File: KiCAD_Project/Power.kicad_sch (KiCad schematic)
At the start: 13 parts, among them J8 NP_Conn_01x02_Relief, J9 NP_Conn_01x02_Relief, U2 1-0000465, U3 1-0000576

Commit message: Issue #2 (NP on all XBEE parts, J3 changed to SMPL)
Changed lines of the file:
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@@
 (kicad_sch
-	(version 20231120)
+	(version 20250114)
 	(generator "eeschema")
-	(generator_version "8.0")
+	(generator_version "9.0")
 	(paper "USLetter")
 	(title_block
@@
 		(comment 2 "Gentry, AR 72734")
 		(comment 3 "23830 West AR Highway 12")
+	)
+	(text "Populate 0R0 and not debounce protection if desired."
+		(exclude_from_sim no)
+		(at 93.345 33.655 0)
+		(effects
+			(font
+				(size 1.27 1.27)
+			)
+			(justify left bottom)
+		)
+	)
+	(text "Delays turn on for approx 1 sec after\npower is applied to help with any\nswitch bounce/activation issues."
+		(exclude_from_sim no)
+		(at 153.035 43.18 0)
+		(effects
+			(font
+				(size 1.27 1.27)
+			)
+			(justify left bottom)
+		)
 	)
 	(junction
@@
 			"k+laF+QKAAACk4RocfgOqvQNL0QGAgBALBISrQq3Gf9cET3hHgAAgBRFq0KdQywM0CoAAEiHpEWr"
 			"wlMS2zYCpOUFAABAIA/RErCspStTZQSHUAEAQMpkKVoyQuk2TeD0AwCAvPh/UbNVz/ggVM8AAAAA"
-			"SUVORK5CYII="
-		)
-	)
-	(text "Populate 0R0 and not debounce protection if desired."
-		(exclude_from_sim no)
-		(at 93.345 33.655 0)
-		(effects
-			(font
-				(size 1.27 1.27)
-			)
-			(justify left bottom)
-		)
-	)
-	(text "Delays turn on for approx 1 sec after\npower is applied to help with any\nswitch bounce/activation issues."
-		(exclude_from_sim no)
-		(at 153.035 43.18 0)
-		(effects
-			(font
-				(size 1.27 1.27)
-			)
-			(justify left bottom)
-		)
-	)
+			"SUVORK5CYIKMADgDgAAAAAAAAAAACAAAAAAAAAAQG6K39gEAAAEAAAAAAAAAAAAAAAAAAABYfn+M"
+			"ADkDgAAAAAAAAAAACAAAAAAAAACQHaK39gEAAAEAAAAAAAAAAAAAAAAAAAAlfniMADoDgAAAAAAA"
+			"AAAAAwAAAAAAAAAgwKm39gEAAAEAAAAAAAAAAAAAAAAAAAAmfgWMADsDgFArqbf2AQAAAwAAAAAA"
+			"AAAgAKW39gEAAAEAAAAAAAAAAAAAAAAAAAAjfgaMADwDgMAhqbf2AQAAAwAAAAAAAADgAKW39gEA"
+			"AAEAAAAAAAAAAAAAAAAAAAAsfgOMAD0DgAAAAAAAAAAAAwAAAAAAAAAwKqm39gEAAAEAAAAAAAAA"
+			"AAAAAAAAAAApfgyMAD4DgAAtqbf2AQAAAwAAAAAAAADAvKm39gEAAAEAAAAAAAAAAAAAAAAAAAAq"
+			"fgmMAD8DgIAiqbf2AQAAAwAAAAAAAACg+qS39gEAAAEAAAAAAAAAAAAAAAAAAAA3fgqMAEADgAAA"
+			"AAAAAAAABAAAAAAAAAABAAAAAAAAAAEAAAAAAAAAAAAAAAAAAAAwfheMAEEDgAAAAAAAAAAAAwAA"
+			"AAAAAAAwvam39gEAAAEAAAAAAAAAAAAAAAAAAAA9fhCMAEIDgAAAAAAAAAAAAwAAAAAAAAAwMKm3"
+			"9gEAAAEAAAAAAAAAAAAAAAAAAAA+fh2MAEMDgCA0qbf2AQAAAwAAAAAAAAAA/KS39gEAAAEAAAAA"
+			"AAAAAAAAAAAAAAA7fh6MAEQDgAA5qbf2AQAAAwAAAAAAAAAA+6S39gEAAAEAAAAAAAAAAAAAAAAA"
+			"AAAEfhuMAEUDgIA0qbf2AQAAAwAAAAAAAADA/KS39gEAAAEAAAAAAAAAAAAAAAAAAAABfiSMAEYD"
+			"gAAAAAAAAAAACAAAAAAAAACQGKK39gEAAAEAAAAAAAAAAAAAAAAAAAACfiGMAEcDgAAAAAAAAAAA"
+			"AwAAAAAAAADgAaW39gEAAAEAAAAAAAAAAAAAAAAAAAAPfiKMAEgDgEM6L1dJTkRPV1MvZm9udHNc"
+			"TklBR0VORy5UVEYAAAAAAAAAAAAAAAAIfi+MAEkDgAAAAAAAAAAABAAAAAAAAAABAAAAAAAAAAEA"
+			"AAAAAAAAAAAAAAAAAAAVfiiMAEoDgAAAAAAAAAAAAwAAAAAAAAAwxKm39gEAAAEAAAAAAAAAAAAA"
+			"AAAAAAAWfjWMAEsDgJAzqbf2AQAAAwAAAAAAAABAvam39gEAAAEAAAAAAAAAAAAAAAAAAAATfjaM"
+			"AEwDgCAuqbf2AQAAAwAAAAAAAABA/KS39gEAAAEAAAAAAAAAAAAAAAAAAAAcfjOMAE0DgAAAAAAA"
+			"AAAABAAAAA=="
+		)
+	)

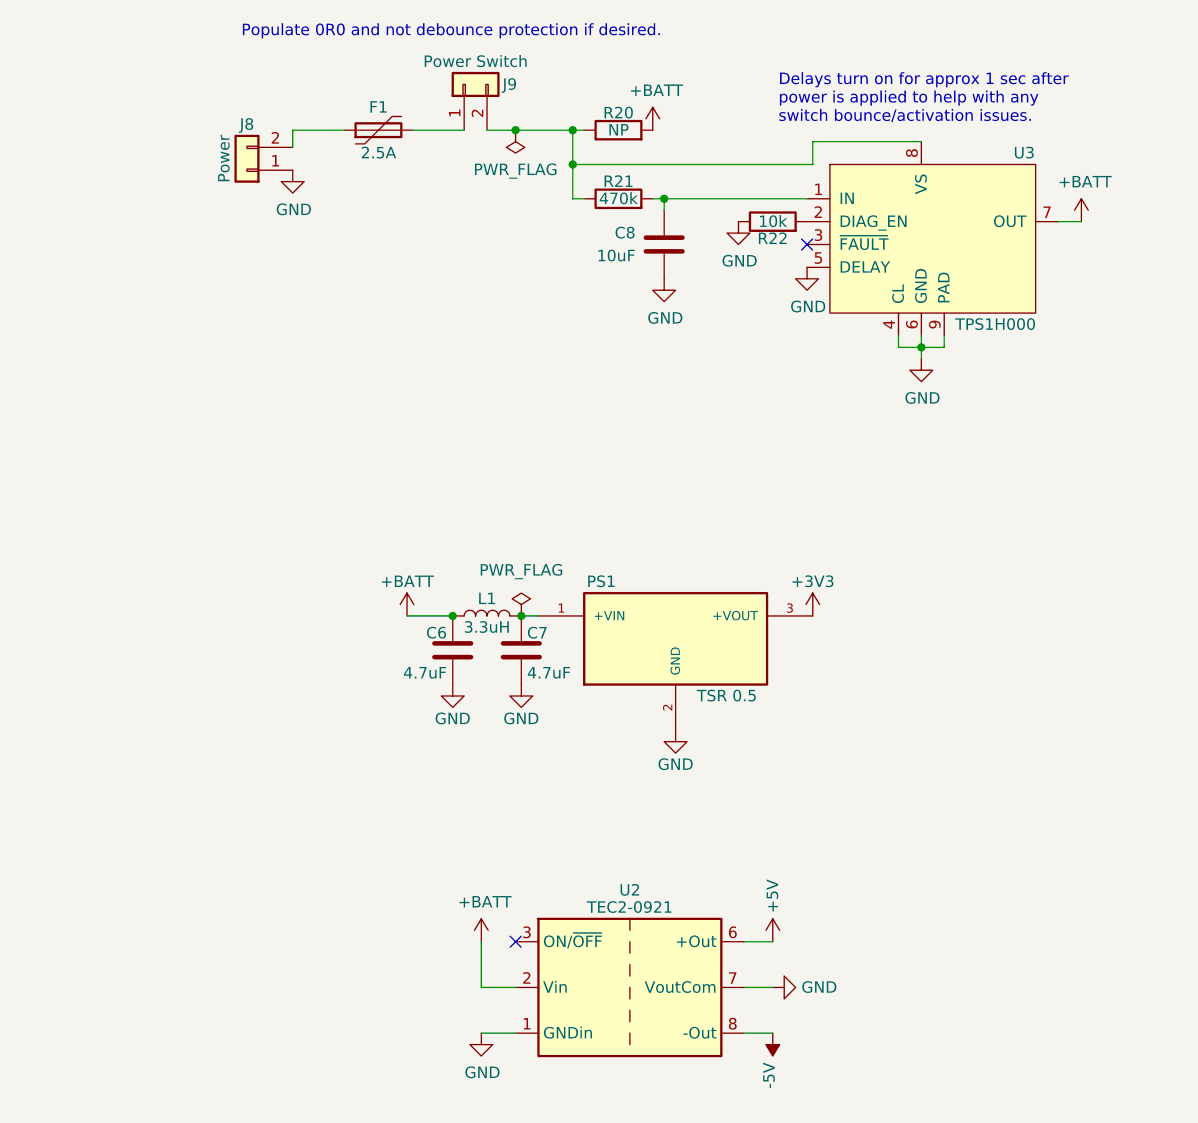
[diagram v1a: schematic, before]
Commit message: Fixed Issue #9 (Added RP Protection)
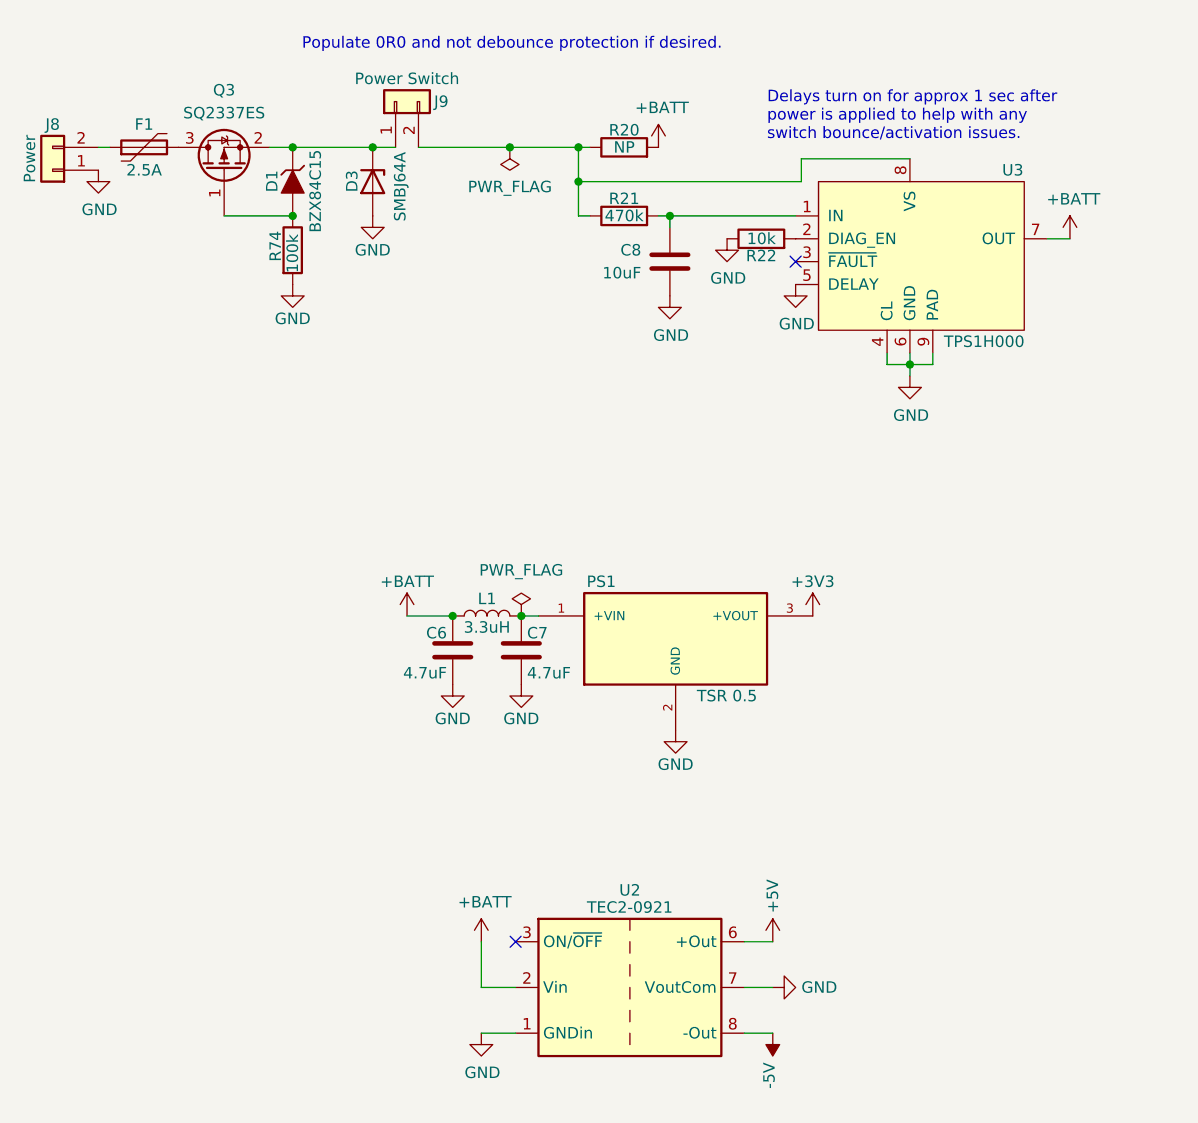
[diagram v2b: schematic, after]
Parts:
- added D1: 1-0001672, diodes:1-0001672, symbol diodes:1-0001672
- added D3: 1-0001537, diodes:1-0001537, symbol diodes:1-0001537
- added Q3: 1-0001670, mosfets:1-0001670, symbol mosfets:1-0001670
- added R74: 1-0000174, resistors_0603:1-0000174, symbol resistors_0603:1-0000174
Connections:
- net GND: now also D3.2 (A), R74.2
- net at F1.2: now also Q3.3 (D); no longer J9.1 (Pin_1)
- new net: D1.1 (A), Q3.1 (G), R74.1
- new net: D1.3 (K), D3.1 (K), J9.1 (Pin_1), Q3.2 (S)
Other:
- moved on the sheet: C8, F1, J8, J9, R20, R21, R22, U3

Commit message: Revised Layout for Rev2.0 Changes
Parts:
- renumbered D3 to D2, J9 to J10, J8 to J9, Q3 to Q1, R74 to R19
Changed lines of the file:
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@@
 	(title_block
 		(title "Digital Rotating Elextronics - NSSL EFM")
-		(date "2024-03-14")
-		(rev "1.0.0")
+		(date "2025-06-10")
+		(rev "2.0.0")
 		(company "Leeman Geophysical LLC")
 		(comment 1 "(479) 373-3736")
@@
 			"AAAAAAAAAAAAAAAAAAAAAAAAAAAAAAAAAKhu1zR+AgAA0NDuTX4CAAAgwhY8fgIAAAAAAAAAAAAA"
 			"AAAAAAAAAAAAAAAAAAAAAAcAAAAAAAAAAAAAAAAAAAAAAAAAAAAAAAAAAAAAAAAAAAAAAAAAAAAA"
-			"AAAAAAAAAA=="
+			"AAAAAAAAAABLlpD3AQAAAAAAAAAAAAAAAAAAAAAAAA8AAAAAAAAAAFCWkPcBAAAAAAAAAAAAAAAA"
+			"AAAAAAAADwAAAAAAAAAAcmlhbCBOYXJyb3cAAAAAAAAAAAAAAAAPAAAAAAAAAAAAAAAAAAAAAAAA"
+			"AAAAAAAAAAAAAAAAAABflpD3AQAAAAAAAAAAAAAAAAAAAAAAAA8AAAAAAAAAAGFycm93IEl0YWxp"
+			"YwAAAAAAAAAAAAAADwAAAAAAAAAAcmlhbCBOYXJyb3cAAAAAAAAAAAAAAAAPAAAAAAAAAAAAAAAA"
+			"AAAAAAAAAAAAAAAAAAAAAAAAAABXlpD3AQAAAAAAAAAAAAAAAAAAAAAAAA8AAAAAAAAAAGFycm93"
+			"AAAAAAAAAAAAAAAAAAAAAAAADwAAAAAAAAAAcmlhbCBOYXJyb3cAAAAAAAAAAAAAAAAPAAAAAAAA"
+			"AAAAAAAAAAAAAAAAAAAAAAAAAAAAAAAAAABOVZD3AQAAAAAAAAAAAAAAAAAAAAAAAA8AAAAAAAAA"
+			"AGFycm93IEJvbGQAAAAAAAAAAAAAAAAADwAAAAAAAAAAcmlhbCBOYXJyb3cAAAAAAAAAAAAAAAAP"
+			"AAAAAAAAAAAAAAAAAAAAAAAAAAAAAAAAAAAAAAAAAADAVJD3AQAAAAAAAAAAAAAAAAAAAAAAAA8A"
+			"AAAAAAAAAMBUkPcBAAAAAAAAAAAAAAAAAAAAAAAADwAAAAAAAAAAcmlhbCBOYXJyb3cAAAAAAAAA"
+			"AAAAAAAPAAAAAAAAAAAAAAAAAAAAAAAAAAAAAAAAAAAAAAAAAAC7VJD3AQAAAAAAAAAAAAAAAAAA"
+			"AAAAAA8AAAAAAAAAAGFycm93IEl0YWxpYwAAAAAAAAAAAAAADwAAAAAAAAAAcmlhbCBOYXJyb3cA"
+			"AAAAAAAAAAAAAAAPAAAAAAAAAAAAAAAAAAAAAAAAAAAAAAAAAAAAAAAAAADLVJD3AQAAAAAAAAAA"
+			"AAAAAAAAAAAAAA8AAAAAAAAAAGFycm93AAAAAAAAAAAAAAAAAAAAAAAADwAAAAAAAAAAcmlhbCBO"
+			"YXJyb3cAAAAAAAAAAAAAAAAPAAAAAAAAAAAAAAAAAAAAAAAAAAAAAAAAAAAAAAAAAABWapD3AQAA"
+			"AAAAAAAAAAAAAAAAAAAAAA8AAAAAAAAAAGFycm93IEJvbGQAAAAAAAAAAAAAAAAADwAAAAAAAAAA"
+			"cmlhbCBOYXJyb3cAAAAAAAAAAAAAAAAPAAAAAAAAAAAAAAAAAAAAAAAAAAAAAAAAAAAAAAAAAACW"
+			"apD3AQAAAAAAAAAAAAAAAAAAAAAAAA8AAAAAAAAAAJdqkPcBAAAAAAAAAAAAAAAAAAAAAAAADwAA"
+			"AAAAAAAAcg=="
 		)
 	)
@@
 		(on_board yes)
 		(dnp no)
-		(property "Reference" "#PWR036"
+		(property "Reference" "#PWR038"
 			(at 111.76 101.6 0)
 			(effects
@@
 			(project "Digital_PCB"
 				(path "/3dbf31f8-25b6-4bae-a8a1-93cabd4e019f/7b8e0205-645d-4360-8e88-d4935c6dfdaa"
-					(reference "#PWR036")
+					(reference "#PWR038")
 					(unit 1)
 				)
@@
 		(on_board yes)
 		(dnp no)
-		(property "Reference" "#PWR047"
+		(property "Reference" "#PWR049"
 			(at 152.4 146.685 0)
 			(effects
@@
 			(project "Digital_PCB"
 				(path "/3dbf31f8-25b6-4bae-a8a1-93cabd4e019f/7b8e0205-645d-4360-8e88-d4935c6dfdaa"
-					(reference "#PWR047")
+					(reference "#PWR049")
 					(unit 1)
 				)
@@
 		(on_board yes)
 		(dnp no)
-		(property "Reference" "#PWR039"
+		(property "Reference" "#PWR041"
 			(at 120.015 150.495 0)
 			(effects
@@
 			(project "Digital_PCB"
 				(path "/3dbf31f8-25b6-4bae-a8a1-93cabd4e019f/7b8e0205-645d-4360-8e88-d4935c6dfdaa"
-					(reference "#PWR039")
+					(reference "#PWR041")
 					(unit 1)
 				)
@@
 		(on_board yes)
 		(dnp no)
-		(property "Reference" "#PWR049"
+		(property "Reference" "#PWR050"
 			(at 154.94 67.31 0)
 			(effects
@@
 			(project "Digital_PCB"
 				(path "/3dbf31f8-25b6-4bae-a8a1-93cabd4e019f/7b8e0205-645d-4360-8e88-d4935c6dfdaa"
-					(reference "#PWR049")
+					(reference "#PWR050")
 					(unit 1)
 				)
@@
 		(on_board yes)
 		(dnp no)
-		(property "Reference" "#PWR043"
+		(property "Reference" "#PWR044"
 			(at 140.97 68.58 0)
 			(effects
@@
 			(project "Digital_PCB"
 				(path "/3dbf31f8-25b6-4bae-a8a1-93cabd4e019f/7b8e0205-645d-4360-8e88-d4935c6dfdaa"
-					(reference "#PWR043")
+					(reference "#PWR044")
 					(unit 1)
 				)
@@
 		(on_board yes)
 		(dnp no)
-		(property "Reference" "R74"
+		(property "Reference" "R19"
 			(at 97.155 58.42 90)
 			(effects
@@
 			(project "Digital_PCB"
 				(path "/3dbf31f8-25b6-4bae-a8a1-93cabd4e019f/7b8e0205-645d-4360-8e88-d4935c6dfdaa"
-					(reference "R74")
+					(reference "R19")
 					(unit 1)
 				)
@@
 		(on_board yes)
 		(dnp no)
-		(property "Reference" "#PWR044"
+		(property "Reference" "#PWR046"
 			(at 147.32 62.23 0)
 			(effects
@@
 			(project "Digital_PCB"
 				(path "/3dbf31f8-25b6-4bae-a8a1-93cabd4e019f/7b8e0205-645d-4360-8e88-d4935c6dfdaa"
-					(reference "#PWR044")
+					(reference "#PWR046")
 					(unit 1)
 				)
@@
 		(on_board yes)
 		(dnp no)
-		(property "Reference" "#PWR041"
+		(property "Reference" "#PWR045"
 			(at 141.605 116.84 0)
 			(effects
@@
 			(project "Digital_PCB"
 				(path "/3dbf31f8-25b6-4bae-a8a1-93cabd4e019f/7b8e0205-645d-4360-8e88-d4935c6dfdaa"
-					(reference "#PWR041")
+					(reference "#PWR045")
 					(unit 1)
 				)
@@
 		(on_board yes)
 		(dnp no)
-		(property "Reference" "#PWR050"
+		(property "Reference" "#PWR052"
 			(at 167.64 77.47 0)
 			(effects
@@
 			(project "Digital_PCB"
 				(path "/3dbf31f8-25b6-4bae-a8a1-93cabd4e019f/7b8e0205-645d-4360-8e88-d4935c6dfdaa"
-					(reference "#PWR050")
+					(reference "#PWR052")
 					(unit 1)
 				)
@@
 		(on_board yes)
 		(dnp no)
-		(property "Reference" "#PWR037"
+		(property "Reference" "#PWR039"
 			(at 116.84 111.76 0)
 			(effects
@@
 			(project "Digital_PCB"
 				(path "/3dbf31f8-25b6-4bae-a8a1-93cabd4e019f/7b8e0205-645d-4360-8e88-d4935c6dfdaa"
-					(reference "#PWR037")
+					(reference "#PWR039")
 					(unit 1)
 				)
@@
 		(on_board yes)
 		(dnp no)
-		(property "Reference" "#PWR038"
+		(property "Reference" "#PWR040"
 			(at 120.015 137.795 0)
 			(effects
@@
 			(project "Digital_PCB"
 				(path "/3dbf31f8-25b6-4bae-a8a1-93cabd4e019f/7b8e0205-645d-4360-8e88-d4935c6dfdaa"
-					(reference "#PWR038")
+					(reference "#PWR040")
 					(unit 1)
 				)
@@
 		(on_board yes)
 		(dnp no)
-		(property "Reference" "#FLG01"
+		(property "Reference" "#FLG02"
 			(at 123.19 47.625 0)
 			(effects
@@
 			(project "Digital_PCB"
 				(path "/3dbf31f8-25b6-4bae-a8a1-93cabd4e019f/7b8e0205-645d-4360-8e88-d4935c6dfdaa"
-					(reference "#FLG01")
+					(reference "#FLG02")
 					(unit 1)
 				)
@@
 		(on_board yes)
 		(dnp no)
-		(property "Reference" "#PWR053"
+		(property "Reference" "#PWR036"
 			(at 99.06 67.31 0)
 			(effects
@@
 			(project "Digital_PCB"
 				(path "/3dbf31f8-25b6-4bae-a8a1-93cabd4e019f/7b8e0205-645d-4360-8e88-d4935c6dfdaa"
-					(reference "#PWR053")
+					(reference "#PWR036")
 					(unit 1)
 				)
@@
 		(on_board yes)
 		(dnp no)
-		(property "Reference" "D3"
+		(property "Reference" "D2"
 			(at 105.664 48.26 0)
 			(effects
@@
 			(project "Digital_PCB"
 				(path "/3dbf31f8-25b6-4bae-a8a1-93cabd4e019f/7b8e0205-645d-4360-8e88-d4935c6dfdaa"
-					(reference "D3")
+					(reference "D2")
 					(unit 1)
 				)
@@
 		(on_board yes)
 		(dnp no)
-		(property "Reference" "#PWR046"
+		(property "Reference" "#PWR048"
 			(at 158.75 139.065 0)
 			(effects
@@
 			(project "Digital_PCB"
 				(path "/3dbf31f8-25b6-4bae-a8a1-93cabd4e019f/7b8e0205-645d-4360-8e88-d4935c6dfdaa"
-					(reference "#PWR046")
+					(reference "#PWR048")
 					(unit 1)
 				)
@@
 		(on_board yes)
 		(dnp no)
-		(property "Reference" "Q3"
+		(property "Reference" "Q1"
 			(at 91.44 39.37 90)
 			(effects
@@
 			(project "Digital_PCB"
 				(path "/3dbf31f8-25b6-4bae-a8a1-93cabd4e019f/7b8e0205-645d-4360-8e88-d4935c6dfdaa"
-					(reference "Q3")
+					(reference "Q1")
 					(unit 1)
 				)
@@
 		(on_board yes)
 		(dnp no)
-		(property "Reference" "#PWR042"
+		(property "Reference" "#PWR043"
 			(at 139.7 49.53 0)
 			(effects
@@
 			(project "Digital_PCB"
 				(path "/3dbf31f8-25b6-4bae-a8a1-93cabd4e019f/7b8e0205-645d-4360-8e88-d4935c6dfdaa"
-					(reference "#PWR042")
+					(reference "#PWR043")
 					(unit 1)
 				)
@@
 		(on_board yes)
 		(dnp no)
-		(property "Reference" "J9"
+		(property "Reference" "J10"
 			(at 115.57 40.64 90)
 			(effects
@@
 			(project "Digital_PCB"
 				(path "/3dbf31f8-25b6-4bae-a8a1-93cabd4e019f/7b8e0205-645d-4360-8e88-d4935c6dfdaa"
-					(reference "J9")
+					(reference "J10")
 					(unit 1)
 				)
@@
 		(on_board yes)
 		(dnp no)
-		(property "Reference" "J8"
+		(property "Reference" "J9"
 			(at 72.39 43.18 0)
 			(effects
@@
 			(project "Digital_PCB"
 				(path "/3dbf31f8-25b6-4bae-a8a1-93cabd4e019f/7b8e0205-645d-4360-8e88-d4935c6dfdaa"
-					(reference "J8")
+					(reference "J9")
 					(unit 1)
 				)
@@
 		(on_board yes)
 		(dnp no)
-		(property "Reference" "#PWR048"
+		(property "Reference" "#PWR051"
 			(at 156.845 101.6 0)
 			(effects
@@
 			(project "Digital_PCB"
 				(path "/3dbf31f8-25b6-4bae-a8a1-93cabd4e019f/7b8e0205-645d-4360-8e88-d4935c6dfdaa"
-					(reference "#PWR048")
+					(reference "#PWR051")
 					(unit 1)
 				)
@@
 		(on_board yes)
 		(dnp no)
-		(property "Reference" "#PWR045"
+		(property "Reference" "#PWR047"
 			(at 152.4 137.795 0)
 			(effects
@@
 			(project "Digital_PCB"
 				(path "/3dbf31f8-25b6-4bae-a8a1-93cabd4e019f/7b8e0205-645d-4360-8e88-d4935c6dfdaa"
-					(reference "#PWR045")
+					(reference "#PWR047")
 					(unit 1)
 				)
@@
 		(on_board yes)
 		(dnp no)
-		(property "Reference" "#PWR040"
+		(property "Reference" "#PWR042"
 			(at 124.46 111.76 0)
 			(effects
@@
 			(project "Digital_PCB"
 				(path "/3dbf31f8-25b6-4bae-a8a1-93cabd4e019f/7b8e0205-645d-4360-8e88-d4935c6dfdaa"
-					(reference "#PWR040")
+					(reference "#PWR042")
 					(unit 1)
 				)
@@
 		(on_board yes)
 		(dnp no)
-		(property "Reference" "#PWR051"
+		(property "Reference" "#PWR053"
 			(at 185.42 59.69 0)
 			(effects
@@
 			(project "Digital_PCB"
 				(path "/3dbf31f8-25b6-4bae-a8a1-93cabd4e019f/7b8e0205-645d-4360-8e88-d4935c6dfdaa"
-					(reference "#PWR051")
+					(reference "#PWR053")
 					(unit 1)
 				)
@@
 		(on_board yes)
 		(dnp no)
-		(property "Reference" "#PWR054"
+		(property "Reference" "#PWR037"
 			(at 107.95 59.69 0)
 			(effects
@@
 			(project "Digital_PCB"
 				(path "/3dbf31f8-25b6-4bae-a8a1-93cabd4e019f/7b8e0205-645d-4360-8e88-d4935c6dfdaa"
-					(reference "#PWR054")
+					(reference "#PWR037")
 					(unit 1)
 				)
